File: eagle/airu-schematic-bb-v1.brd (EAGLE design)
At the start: 86.4 x 54.6 mm, 26 parts, among them U1 BMP180, U2 DHT22, U3 GPS, X2 53261-08

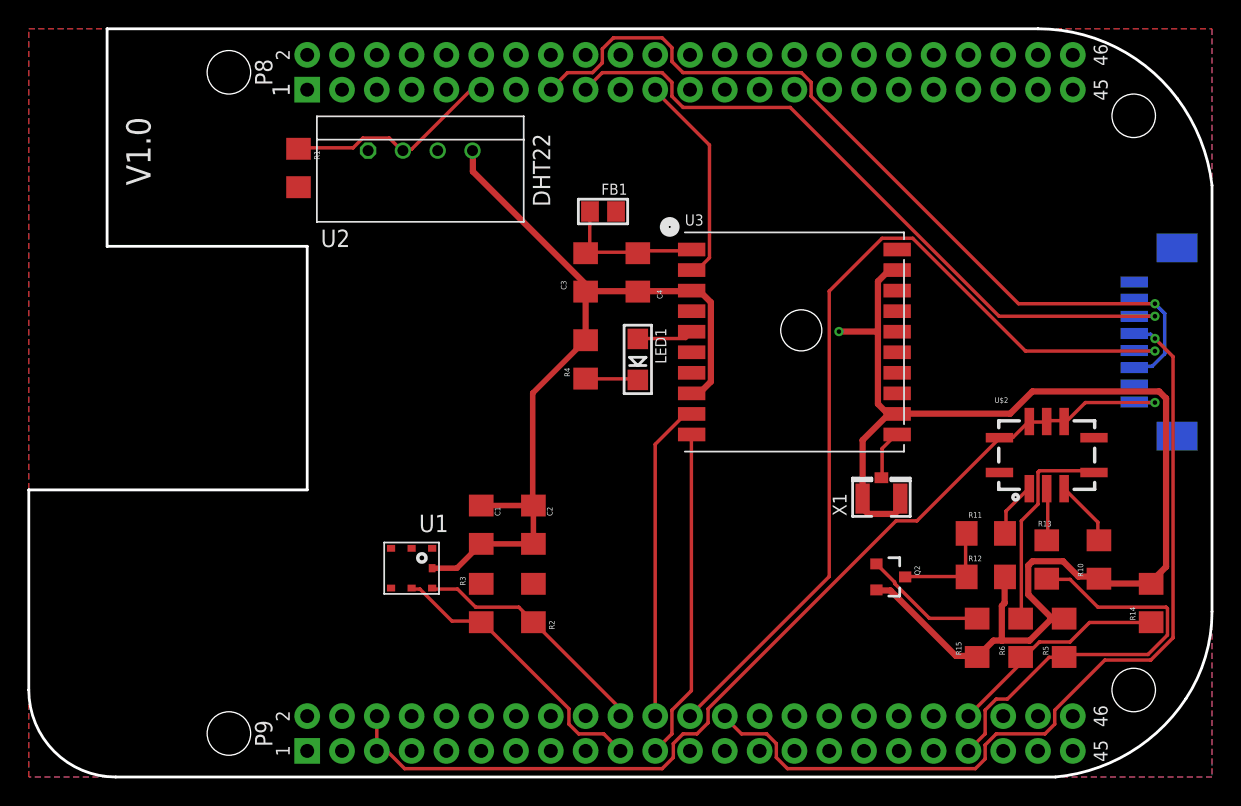
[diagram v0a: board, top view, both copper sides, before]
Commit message: Made improvements to layout and added silkscreen components.
This commit includes improvments to the physical layout as well as
comments on the silkscreen layer.
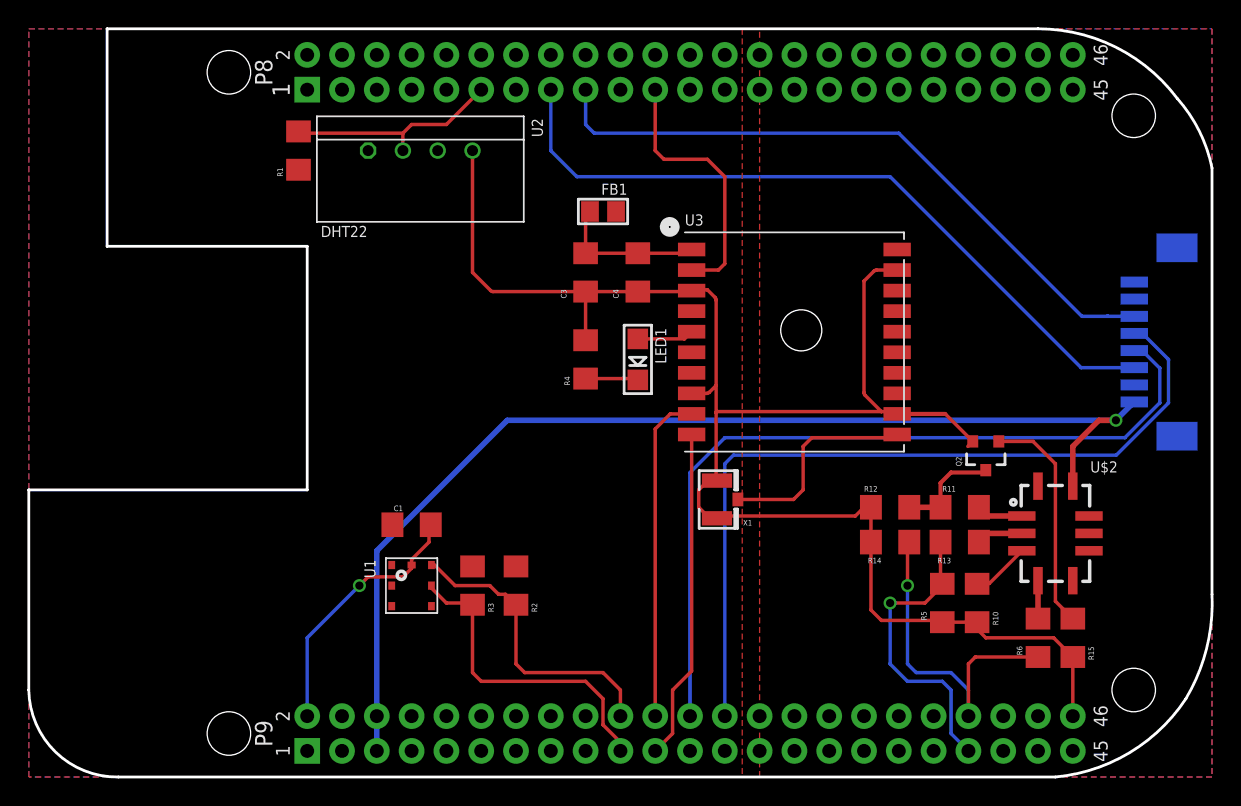
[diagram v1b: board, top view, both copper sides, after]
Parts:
- removed C2: 0.1uF, SparkFun-Passives:1206
- R13: value 449 -> 453
- moved R14 19.6 mm to (62.9, 17.1), turned to 0 degrees
- moved X1 12.0 mm to (50.2, 20.3), turned to 0 degrees
- moved Q2 11.3 mm to (69.8, 23.5), turned to 180 degrees
- moved R10 9.44 mm to (69.2, 12.7)
- moved R5 9.25 mm to (66.7, 12.7), turned to 90 degrees
- moved R12 8.64 mm to (62.9, 19.7), turned to 0 degrees
- moved R15 6.98 mm to (76.2, 10.2)
- moved R13 6.48 mm to (67.9, 17.1), turned to 0 degrees
- moved U$2 5.75 mm to (74.9, 17.8), turned to 90 degrees
- moved C1 5.08 mm to (27.9, 18.4), turned to 0 degrees
- moved R11 2.69 mm to (67.9, 19.7)
- moved R2 1.80 mm to (35.6, 14.0)
- moved R3 1.42 mm to (32.4, 14.0)
- moved U1 1.27 mm to (27.9, 14.0), turned to 90 degrees
- moved R1 1.27 mm to (19.7, 45.7)
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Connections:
- net BMP_SCL renamed SCL
- net BMP_SDA renamed SDA
- net 3.3V: no longer C2.1
- net GND: no longer C2.2
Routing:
- net GND: track 157.2 -> 143.1 mm
- net N$8: track 15.4 -> 2.77 mm
- net N$2: track 3.66 -> 15.5 mm
- net VRED: track 16.5 -> 25.3 mm, vias 0 -> 1
- net PM_SET: track 62.1 -> 53.6 mm, vias 1 -> 0
- net VOX: track 30.7 -> 22.2 mm, vias 0 -> 1
- net 5V: track 73.7 -> 81.9 mm
- net PRE_HEAT_NOX: track 9.06 -> 16.6 mm
- net PM_RXD: track 65.5 -> 59.1 mm, vias 1 -> 0
- net PM_TXD: track 64.1 -> 59.1 mm, vias 1 -> 0
- net SDA: track 18.0 -> 22.0 mm
- net 3.3V: track 3.81 -> 0.00 mm
- net GPS_NRST: track 15.6 -> 19.3 mm
- net PM_RESET: track 51.6 -> 48.4 mm, vias 1 -> 0
- net SCL: track 20.9 -> 23.3 mm
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- added copper zone on layer 1, net 5V
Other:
- outline, holes or cut-outs redrawn
- board text added: "02/2016 Jonathan Whitaker"
